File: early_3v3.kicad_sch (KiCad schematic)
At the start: 5 parts, among them U1301 SE8633K2-HF

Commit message: Apply part PCBA position corrections
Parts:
- U1301: JLCPCB_CORRECTION (none) -> -0.5;0;180
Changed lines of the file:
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@@
+			)
+		)
+		(property "JLCPCB_CORRECTION" "-0.5;0;180"
+			(at 143.51 68.58 0)
+			(effects
+				(font
+					(size 1.27 1.27)
+				)
+				(hide yes)
 			)
 		)

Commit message: Reannotate the board
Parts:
- renumbered C1304 to C53, C1307 to C54, D1404 to D13, D2602 to D14, U1301 to U11
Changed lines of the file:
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@@
 		(dnp no)
 		(fields_autoplaced yes)
-		(property "Reference" "D1404"
+		(property "Reference" "D13"
 			(at 193.3575 49.53 0)
 			(effects
@@
 			(project "HALPI2"
 				(path "/abc482bd-3f17-4d35-80db-1da3dcdb5c27/c7bf4e1f-6bd1-4be7-9e56-1bd438bf5d42/8e6a478f-fb3c-4be6-a57a-6d17571606cc"
-					(reference "D1404")
+					(reference "D13")
 					(unit 1)
 				)
@@
 		(dnp no)
 		(fields_autoplaced yes)
-		(property "Reference" "D2602"
+		(property "Reference" "D14"
 			(at 193.04 62.23 0)
 			(effects
@@
 			(project "HALPI2"
 				(path "/abc482bd-3f17-4d35-80db-1da3dcdb5c27/c7bf4e1f-6bd1-4be7-9e56-1bd438bf5d42/8e6a478f-fb3c-4be6-a57a-6d17571606cc"
-					(reference "D2602")
+					(reference "D14")
 					(unit 1)
 				)
@@
 		(dnp no)
 		(fields_autoplaced yes)
-		(property "Reference" "#PWR01315"
+		(property "Reference" "#PWR070"
 			(at 120.65 83.82 0)
 			(effects
@@
 			(project "HALPI2"
 				(path "/abc482bd-3f17-4d35-80db-1da3dcdb5c27/c7bf4e1f-6bd1-4be7-9e56-1bd438bf5d42/8e6a478f-fb3c-4be6-a57a-6d17571606cc"
-					(reference "#PWR01315")
+					(reference "#PWR070")
 					(unit 1)
 				)
@@
 		(dnp no)
 		(fields_autoplaced yes)
-		(property "Reference" "#PWR01314"
+		(property "Reference" "#PWR074"
 			(at 218.44 57.15 0)
 			(effects
@@
 			(project "HALPI2"
 				(path "/abc482bd-3f17-4d35-80db-1da3dcdb5c27/c7bf4e1f-6bd1-4be7-9e56-1bd438bf5d42/8e6a478f-fb3c-4be6-a57a-6d17571606cc"
-					(reference "#PWR01314")
+					(reference "#PWR074")
 					(unit 1)
 				)
@@
 		(dnp no)
 		(fields_autoplaced yes)
-		(property "Reference" "C1304"
+		(property "Reference" "C53"
 			(at 124.46 72.3899 0)
 			(effects
@@
 			(project "HALPI2"
 				(path "/abc482bd-3f17-4d35-80db-1da3dcdb5c27/c7bf4e1f-6bd1-4be7-9e56-1bd438bf5d42/8e6a478f-fb3c-4be6-a57a-6d17571606cc"
-					(reference "C1304")
+					(reference "C53")
 					(unit 1)
 				)
@@
 		(dnp no)
 		(fields_autoplaced yes)
-		(property "Reference" "#PWR01312"
+		(property "Reference" "#PWR072"
 			(at 160.02 83.82 0)
 			(effects
@@
 			(project "HALPI2"
 				(path "/abc482bd-3f17-4d35-80db-1da3dcdb5c27/c7bf4e1f-6bd1-4be7-9e56-1bd438bf5d42/8e6a478f-fb3c-4be6-a57a-6d17571606cc"
-					(reference "#PWR01312")
+					(reference "#PWR072")
 					(unit 1)
 				)
@@
 		(dnp no)
 		(fields_autoplaced yes)
-		(property "Reference" "#PWR01301"
+		(property "Reference" "#PWR073"
 			(at 182.88 57.15 0)
 			(effects
@@
 			(project ""
 				(path "/abc482bd-3f17-4d35-80db-1da3dcdb5c27/c7bf4e1f-6bd1-4be7-9e56-1bd438bf5d42/8e6a478f-fb3c-4be6-a57a-6d17571606cc"
-					(reference "#PWR01301")
+					(reference "#PWR073")
 					(unit 1)
 				)
@@
 		(on_board yes)
 		(dnp no)
-		(property "Reference" "C1307"
+		(property "Reference" "C54"
 			(at 162.941 71.2216 0)
 			(effects
@@
 			(project "HALPI2"
 				(path "/abc482bd-3f17-4d35-80db-1da3dcdb5c27/c7bf4e1f-6bd1-4be7-9e56-1bd438bf5d42/8e6a478f-fb3c-4be6-a57a-6d17571606cc"
-					(reference "C1307")
+					(reference "C54")
 					(unit 1)
 				)
@@
 		(dnp no)
 		(fields_autoplaced yes)
-		(property "Reference" "U1301"
+		(property "Reference" "U11"
 			(at 143.51 62.23 0)
 			(effects
@@
 			(project ""
 				(path "/abc482bd-3f17-4d35-80db-1da3dcdb5c27/c7bf4e1f-6bd1-4be7-9e56-1bd438bf5d42/8e6a478f-fb3c-4be6-a57a-6d17571606cc"
-					(reference "U1301")
+					(reference "U11")
 					(unit 1)
 				)
@@
 		(dnp no)
 		(fields_autoplaced yes)
-		(property "Reference" "#FLG01301"
+		(property "Reference" "#FLG010"
 			(at 220.345 62.23 0)
 			(effects
@@
 			(project ""
 				(path "/abc482bd-3f17-4d35-80db-1da3dcdb5c27/c7bf4e1f-6bd1-4be7-9e56-1bd438bf5d42/8e6a478f-fb3c-4be6-a57a-6d17571606cc"
-					(reference "#FLG01301")
+					(reference "#FLG010")
 					(unit 1)
 				)
@@
 		(dnp no)
 		(fields_autoplaced yes)
-		(property "Reference" "#PWR01313"
+		(property "Reference" "#PWR071"
 			(at 143.51 83.82 0)
 			(effects
@@
 			(project "HALPI2"
 				(path "/abc482bd-3f17-4d35-80db-1da3dcdb5c27/c7bf4e1f-6bd1-4be7-9e56-1bd438bf5d42/8e6a478f-fb3c-4be6-a57a-6d17571606cc"
-					(reference "#PWR01313")
-					(unit 1)
-				)
+					(reference "#PWR071")
+					(unit 1)
+				)

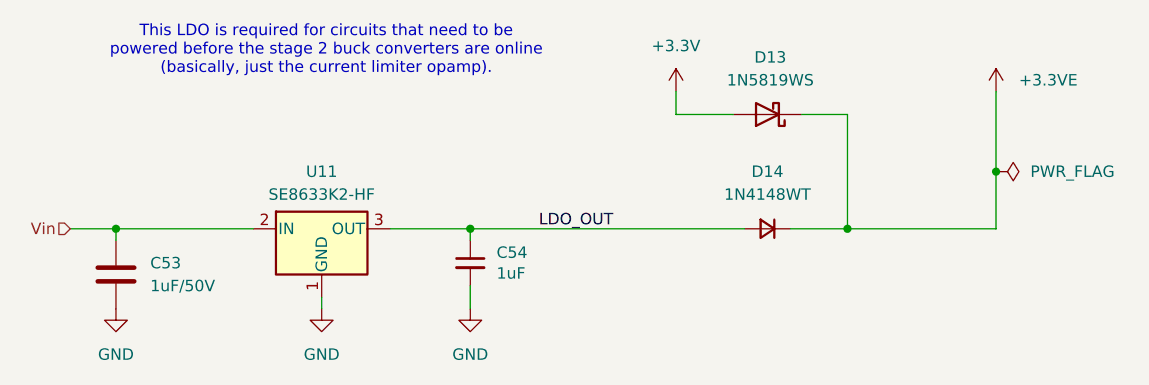
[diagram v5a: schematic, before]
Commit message: Add GND/3.3V/5V headers, add missing JLC part numbers
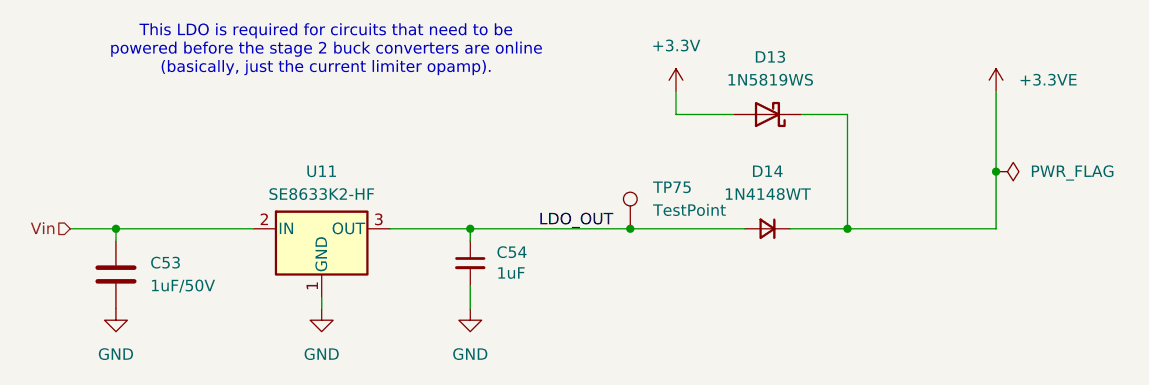
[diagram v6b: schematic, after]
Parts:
- added TP75: TestPoint, TestPoint:TestPoint_Pad_D1.0mm, symbol Connector:TestPoint
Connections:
- net LDO_OUT: now also TP75.1
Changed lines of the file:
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@@
+	)
+	(junction
+		(at 177.8 68.58)
+		(diameter 0)
+		(color 0 0 0 0)
 	)
 	(junction
@@
 	(wire
 		(pts
+			(xy 177.8 68.58) (xy 190.5 68.58)
+		)
+		(stroke
+			(width 0)
+			(type default)
+		)
+	)
+	(wire
+		(pts
 			(xy 218.44 53.34) (xy 218.44 62.23)
 		)
@@
 	(wire
 		(pts
-			(xy 160.02 68.58) (xy 190.5 68.58)
+			(xy 160.02 68.58) (xy 177.8 68.58)
 		)
 		(stroke
@@
 				)
 			)
+		)
+	)
+	(symbol
+		(lib_id "Connector:TestPoint")
+		(at 177.8 68.58 0)
+		(unit 1)
+		(exclude_from_sim no)
+		(in_bom yes)
+		(on_board yes)
+		(dnp no)
+		(fields_autoplaced yes)
+		(property "Reference" "TP75"
+			(at 180.34 64.0079 0)
+			(effects
+				(font
+					(size 1.27 1.27)
+				)
+				(justify left)
+			)
+		)
+		(property "Value" "TestPoint"
+			(at 180.34 66.5479 0)
+			(effects
+				(font
+					(size 1.27 1.27)
+				)
+				(justify left)
+			)
+		)
+		(property "Footprint" "TestPoint:TestPoint_Pad_D1.0mm"
+			(at 182.88 68.58 0)
+			(effects
+				(font
+					(size 1.27 1.27)
+				)
+				(hide yes)
+			)
+		)
+		(property "Datasheet" "~"
+			(at 182.88 68.58 0)
+			(effects
+				(font
+					(size 1.27 1.27)
+				)
+				(hide yes)
+			)
+		)
+		(property "Description" "test point"
+			(at 177.8 68.58 0)
+			(effects
+				(font
+					(size 1.27 1.27)
+				)
+				(hide yes)
+			)
+		)
+		(pin "1"
+		)
+		(instances
+			(project "HALPI2"
+				(path "/abc482bd-3f17-4d35-80db-1da3dcdb5c27/c7bf4e1f-6bd1-4be7-9e56-1bd438bf5d42/8e6a478f-fb3c-4be6-a57a-6d17571606cc"
+					(reference "TP75")
+					(unit 1)
+				)
+			)

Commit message: FInal v0.2.0 proto changes
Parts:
- D13: renamed from D14; JLCPCB_CORRECTION (none) -> 0;0;180
- renumbered C53 to C55, C54 to C56, D13 to D12, TP75 to TP32
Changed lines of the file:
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@@
 		(dnp no)
 		(fields_autoplaced yes)
-		(property "Reference" "TP75"
+		(property "Reference" "TP32"
 			(at 180.34 64.0079 0)
 			(effects
@@
 			)
 		)
+		(property "Sim.Enable" ""
+			(at 177.8 68.58 0)
+			(effects
+				(font
+					(size 1.27 1.27)
+				)
+			)
+		)
 		(pin "1"
 		)
@@
 			(project "HALPI2"
 				(path "/abc482bd-3f17-4d35-80db-1da3dcdb5c27/c7bf4e1f-6bd1-4be7-9e56-1bd438bf5d42/8e6a478f-fb3c-4be6-a57a-6d17571606cc"
-					(reference "TP75")
+					(reference "TP32")
 					(unit 1)
 				)
@@
 		(dnp no)
 		(fields_autoplaced yes)
-		(property "Reference" "D13"
+		(property "Reference" "D12"
 			(at 193.3575 49.53 0)
 			(effects
@@
 			(project "HALPI2"
 				(path "/abc482bd-3f17-4d35-80db-1da3dcdb5c27/c7bf4e1f-6bd1-4be7-9e56-1bd438bf5d42/8e6a478f-fb3c-4be6-a57a-6d17571606cc"
-					(reference "D13")
+					(reference "D12")
 					(unit 1)
 				)
@@
 		(dnp no)
 		(fields_autoplaced yes)
-		(property "Reference" "D14"
+		(property "Reference" "D13"
 			(at 193.04 62.23 0)
 			(effects
@@
 			)
 		)
+		(property "JLCPCB_CORRECTION" "0;0;180"
+			(at 193.04 68.58 0)
+			(effects
+				(font
+					(size 1.27 1.27)
+				)
+			)
+		)
 		(pin "2"
 		)
@@
 			(project "HALPI2"
 				(path "/abc482bd-3f17-4d35-80db-1da3dcdb5c27/c7bf4e1f-6bd1-4be7-9e56-1bd438bf5d42/8e6a478f-fb3c-4be6-a57a-6d17571606cc"
-					(reference "D14")
+					(reference "D13")
 					(unit 1)
 				)
@@
 		(dnp no)
 		(fields_autoplaced yes)
-		(property "Reference" "#PWR070"
+		(property "Reference" "#PWR071"
 			(at 120.65 83.82 0)
 			(effects
@@
 			(project "HALPI2"
 				(path "/abc482bd-3f17-4d35-80db-1da3dcdb5c27/c7bf4e1f-6bd1-4be7-9e56-1bd438bf5d42/8e6a478f-fb3c-4be6-a57a-6d17571606cc"
-					(reference "#PWR070")
+					(reference "#PWR071")
 					(unit 1)
 				)
@@
 		(dnp no)
 		(fields_autoplaced yes)
-		(property "Reference" "#PWR074"
+		(property "Reference" "#PWR075"
 			(at 218.44 57.15 0)
 			(effects
@@
 			(project "HALPI2"
 				(path "/abc482bd-3f17-4d35-80db-1da3dcdb5c27/c7bf4e1f-6bd1-4be7-9e56-1bd438bf5d42/8e6a478f-fb3c-4be6-a57a-6d17571606cc"
-					(reference "#PWR074")
+					(reference "#PWR075")
 					(unit 1)
 				)
@@
 		(dnp no)
 		(fields_autoplaced yes)
-		(property "Reference" "C53"
+		(property "Reference" "C55"
 			(at 124.46 72.3899 0)
 			(effects
@@
 			(project "HALPI2"
 				(path "/abc482bd-3f17-4d35-80db-1da3dcdb5c27/c7bf4e1f-6bd1-4be7-9e56-1bd438bf5d42/8e6a478f-fb3c-4be6-a57a-6d17571606cc"
-					(reference "C53")
+					(reference "C55")
 					(unit 1)
 				)
@@
 		(dnp no)
 		(fields_autoplaced yes)
-		(property "Reference" "#PWR072"
+		(property "Reference" "#PWR073"
 			(at 160.02 83.82 0)
 			(effects
@@
 			(project "HALPI2"
 				(path "/abc482bd-3f17-4d35-80db-1da3dcdb5c27/c7bf4e1f-6bd1-4be7-9e56-1bd438bf5d42/8e6a478f-fb3c-4be6-a57a-6d17571606cc"
-					(reference "#PWR072")
+					(reference "#PWR073")
 					(unit 1)
 				)
@@
 		(dnp no)
 		(fields_autoplaced yes)
-		(property "Reference" "#PWR073"
+		(property "Reference" "#PWR074"
 			(at 182.88 57.15 0)
 			(effects
@@
 			(project ""
 				(path "/abc482bd-3f17-4d35-80db-1da3dcdb5c27/c7bf4e1f-6bd1-4be7-9e56-1bd438bf5d42/8e6a478f-fb3c-4be6-a57a-6d17571606cc"
-					(reference "#PWR073")
+					(reference "#PWR074")
 					(unit 1)
 				)
@@
 		(on_board yes)
 		(dnp no)
-		(property "Reference" "C54"
+		(property "Reference" "C56"
 			(at 162.941 71.2216 0)
 			(effects
@@
 			(project "HALPI2"
 				(path "/abc482bd-3f17-4d35-80db-1da3dcdb5c27/c7bf4e1f-6bd1-4be7-9e56-1bd438bf5d42/8e6a478f-fb3c-4be6-a57a-6d17571606cc"
-					(reference "C54")
+					(reference "C56")
 					(unit 1)
 				)
@@
 		(dnp no)
 		(fields_autoplaced yes)
-		(property "Reference" "#PWR071"
+		(property "Reference" "#PWR072"
 			(at 143.51 83.82 0)
 			(effects
@@
 			(project "HALPI2"
 				(path "/abc482bd-3f17-4d35-80db-1da3dcdb5c27/c7bf4e1f-6bd1-4be7-9e56-1bd438bf5d42/8e6a478f-fb3c-4be6-a57a-6d17571606cc"
-					(reference "#PWR071")
-					(unit 1)
-				)
+					(reference "#PWR072")
+					(unit 1)
+				)
